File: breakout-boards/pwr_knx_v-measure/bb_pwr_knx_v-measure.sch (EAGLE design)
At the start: 47 parts, among them IC100 BD9G101, T1 BC856, T2 BCP52, T3 BC847

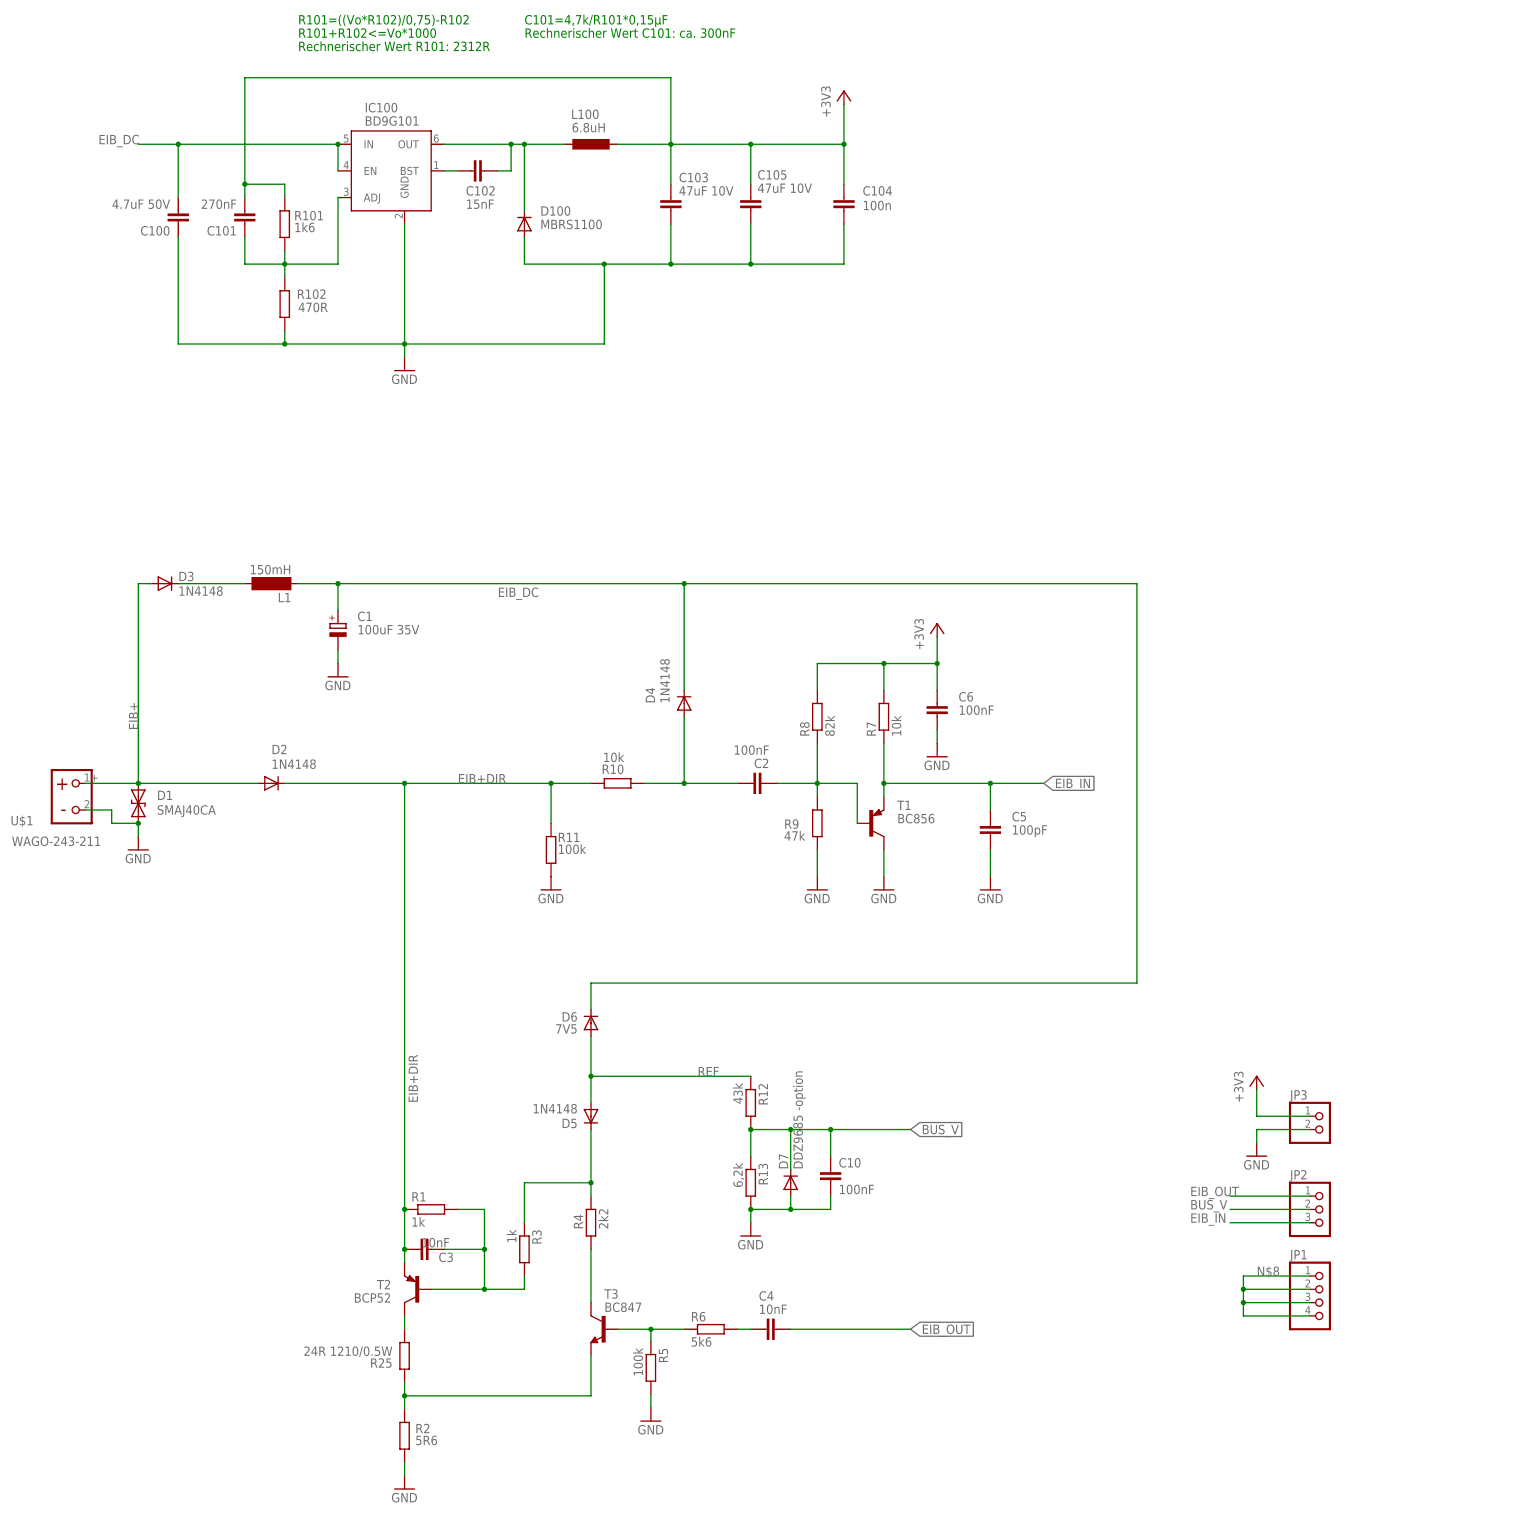
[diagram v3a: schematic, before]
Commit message: [BB_Pwr+KNX] - update pin positions
accidentially committed a version with old pin positions yesterday
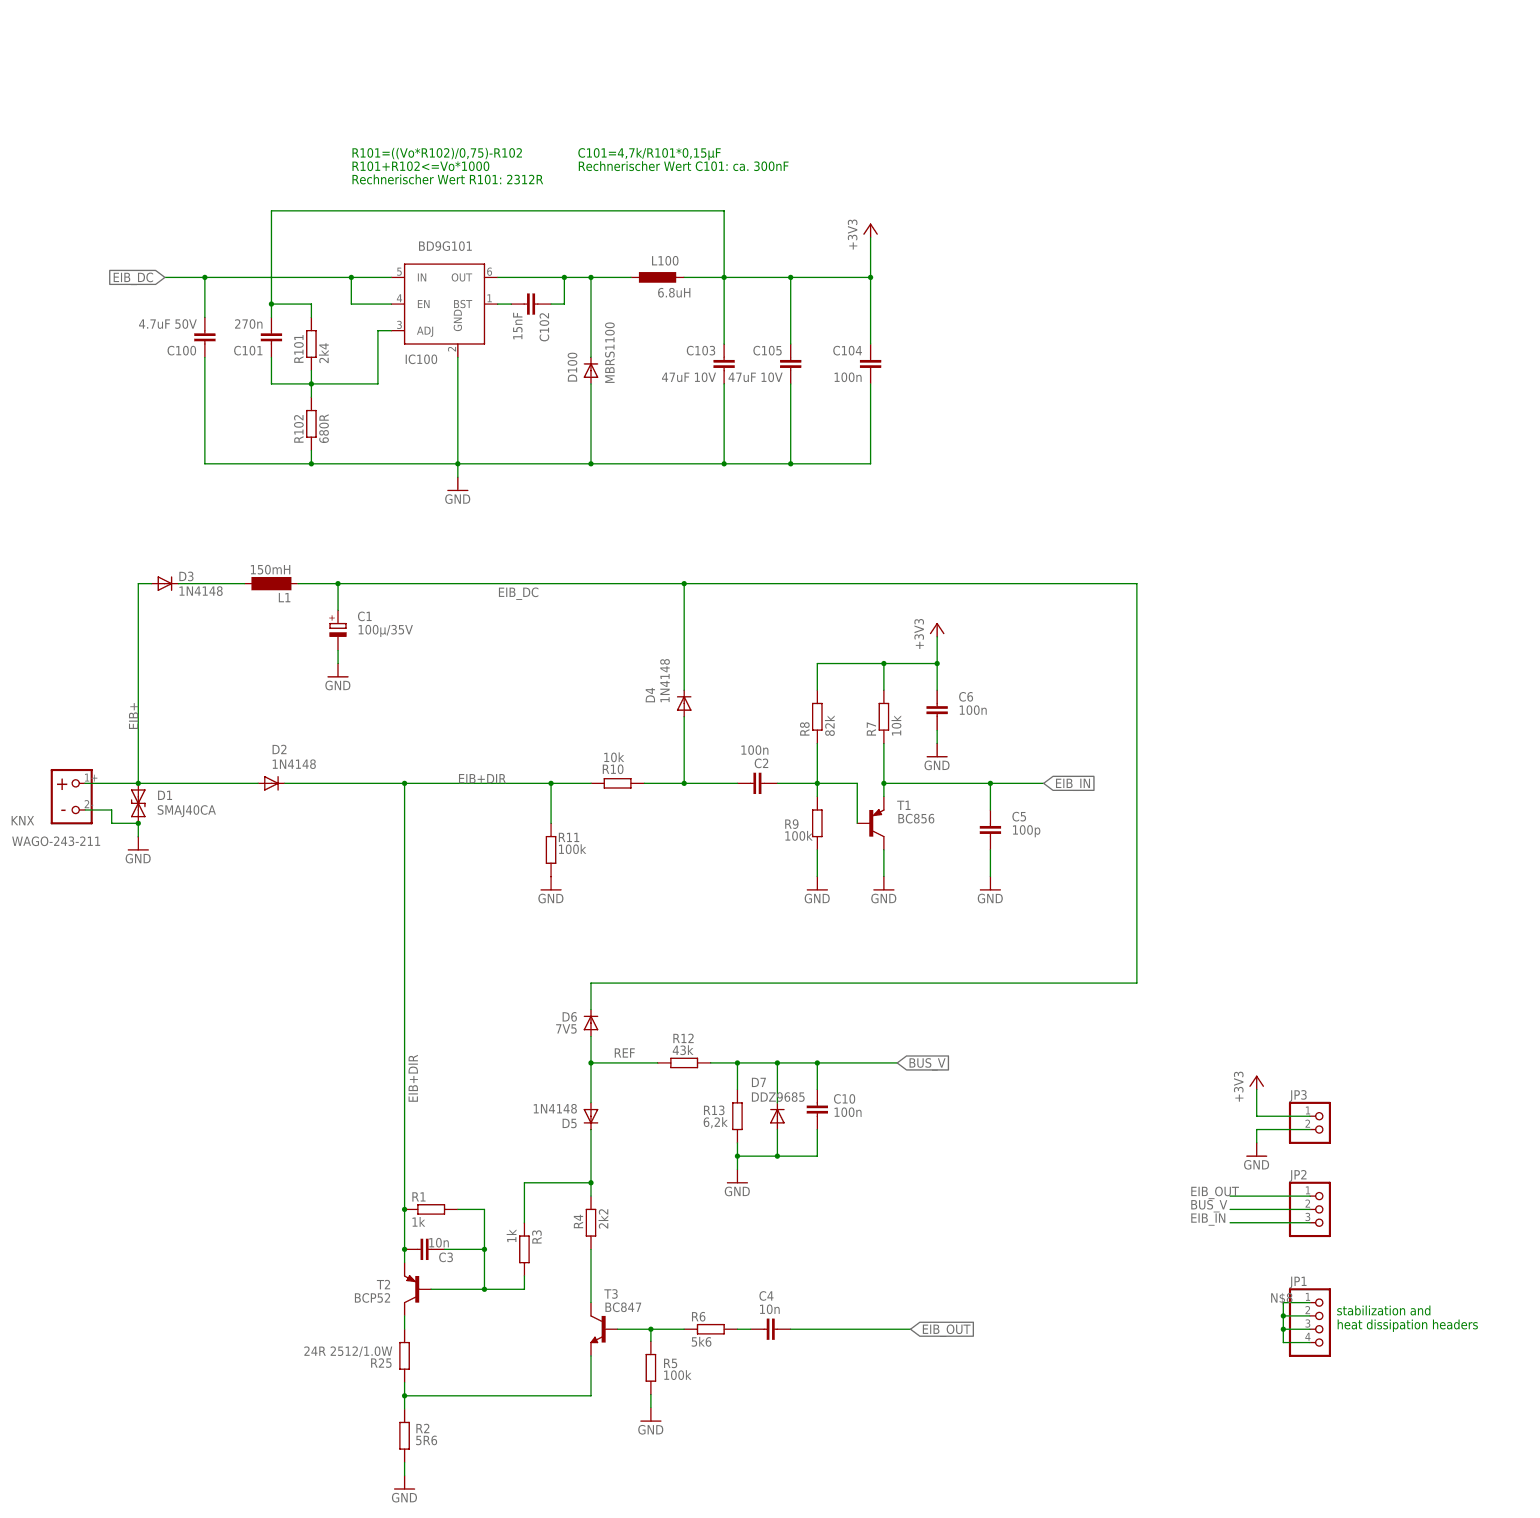
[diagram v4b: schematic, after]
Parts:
- C1: value 100uF 35V -> 100µ/35V
- C10, C2, C6: value 100nF -> 100n
- C100: REICHELT (none) -> X7R-G1206 4,7/50
- C101: value 270nF -> 270n
- C102: REICHELT (none) -> X7R-G0805 15N
- C3, C4: value 10nF -> 10n
- C5: value 100pF -> 100p
- D3: REICHELT (none) -> 1N 4148 SMD
- D7: value DDZ9685 -option -> DDZ9685
- R101: value 1k6 -> 2k4
- R102: value 470R -> 680R
- R25: value 24R 1210/0.5W -> 24R 2512/1.0W
- R6: REICHELT (none) -> SMD-0805 5,60K
- R9: value 47k -> 100k
- T3: REICHELT (none) -> BC 847C SMD
- renumbered U$1 to KNX
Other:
- note added: "stabilization and heat dissipation headers"
- moved on the sheet: C10, C100, C101, C102, C103, C104, C105, D100, D7, IC100, JP1, L100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

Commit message: [BB_Pwr+KNX] - updated docu; updated values of buck components
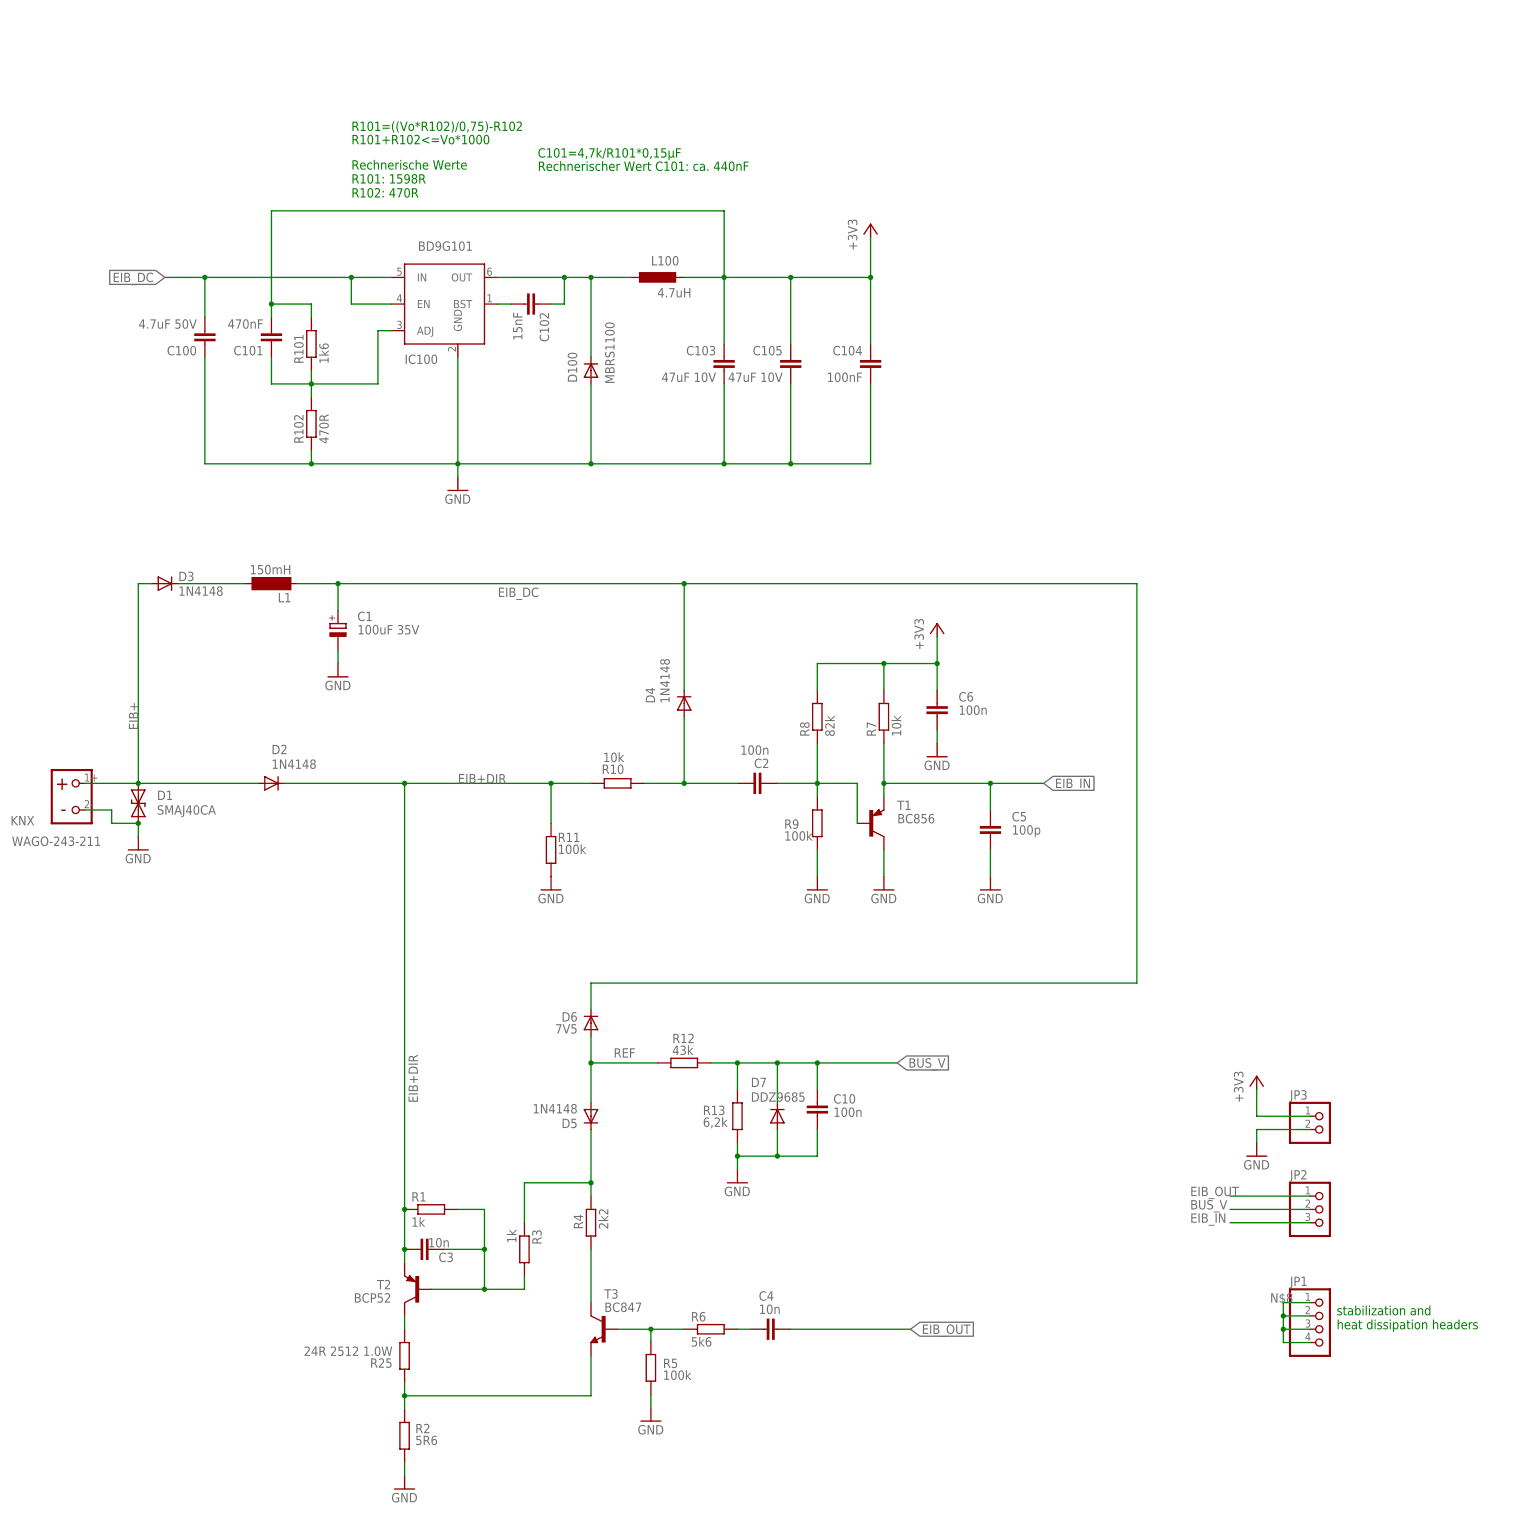
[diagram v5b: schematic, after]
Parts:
- C1: value 100µ/35V -> 100uF 35V
- C101: value 270n -> 470nF
- C104: value 100n -> 100nF
- D3: REICHELT 1N 4148 SMD -> (none)
- L100: value 6.8uH -> 4.7uH
- R101: value 2k4 -> 1k6
- R102: value 680R -> 470R
- R25: value 24R 2512/1.0W -> 24R 2512 1.0W
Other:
- note added: "Rechnerische Werte R101: 1598R R102: 470R"
- note added: "Rechnerischer Wert C101: ca. 440nF"
- note removed: "Rechnerischer Wert C101: ca. 300nF"
- note removed: "Rechnerischer Wert R101: 2312R"
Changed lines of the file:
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@@
 <parts>
 <part name="GND4" library="supply1" deviceset="GND" device=""/>
-<part name="C104" library="rcl" library_urn="urn:adsk.eagle:library:334" deviceset="C-EU" device="C0805" package3d_urn="urn:adsk.eagle:package:23617/2" value="100n">
+<part name="C104" library="rcl" library_urn="urn:adsk.eagle:library:334" deviceset="C-EU" device="C0805" package3d_urn="urn:adsk.eagle:package:23617/2" value="100nF">
 <spice>
 <pinmapping spiceprefix="C">
@@
 <part name="P+3" library="supply1" deviceset="+3V3" device=""/>
 <part name="IC100" library="Stefan_selfbus" deviceset="BD9G101G" device="BD9G101G-SOT23-6" value="BD9G101"/>
-<part name="L100" library="rcl_changed" deviceset="L-EU" device="L4532P" package3d_urn="urn:adsk.eagle:package:23484/1" value="6.8uH">
+<part name="L100" library="rcl_changed" deviceset="L-EU" device="L4532P" package3d_urn="urn:adsk.eagle:package:23484/1" value="4.7uH">
 <spice>
 <pinmapping spiceprefix="L">
@@
 <attribute name="REICHELT" value="X7R-G0805 15N"/>
 </part>
-<part name="R101" library="rcl" library_urn="urn:adsk.eagle:library:334" deviceset="R-EU_" device="R0805" package3d_urn="urn:adsk.eagle:package:23553/2" value="2k4">
-<spice>
-<pinmapping spiceprefix="R">
-<pinmap gate="G$1" pin="1" pinorder="1"/>
-<pinmap gate="G$1" pin="2" pinorder="2"/>
-</pinmapping>
-</spice>
-</part>
-<part name="R102" library="rcl" library_urn="urn:adsk.eagle:library:334" deviceset="R-EU_" device="R0805" package3d_urn="urn:adsk.eagle:package:23553/2" value="680R">
-<spice>
-<pinmapping spiceprefix="R">
-<pinmap gate="G$1" pin="1" pinorder="1"/>
-<pinmap gate="G$1" pin="2" pinorder="2"/>
-</pinmapping>
-</spice>
-</part>
-<part name="C101" library="rcl" library_urn="urn:adsk.eagle:library:334" deviceset="C-EU" device="C0805" package3d_urn="urn:adsk.eagle:package:23617/2" value="270n">
+<part name="R101" library="rcl" library_urn="urn:adsk.eagle:library:334" deviceset="R-EU_" device="R0805" package3d_urn="urn:adsk.eagle:package:23553/2" value="1k6">
+<spice>
+<pinmapping spiceprefix="R">
+<pinmap gate="G$1" pin="1" pinorder="1"/>
+<pinmap gate="G$1" pin="2" pinorder="2"/>
+</pinmapping>
+</spice>
+</part>
+<part name="R102" library="rcl" library_urn="urn:adsk.eagle:library:334" deviceset="R-EU_" device="R0805" package3d_urn="urn:adsk.eagle:package:23553/2" value="470R">
+<spice>
+<pinmapping spiceprefix="R">
+<pinmap gate="G$1" pin="1" pinorder="1"/>
+<pinmap gate="G$1" pin="2" pinorder="2"/>
+</pinmapping>
+</spice>
+</part>
+<part name="C101" library="rcl" library_urn="urn:adsk.eagle:library:334" deviceset="C-EU" device="C0805" package3d_urn="urn:adsk.eagle:package:23617/2" value="470nF">
 <spice>
 <pinmapping spiceprefix="C">
@@
 </spice>
 </part>
-<part name="C1" library="rcl" library_urn="urn:adsk.eagle:library:334" deviceset="CPOL-EU" device="SANYO_SMD_C6" package3d_urn="urn:adsk.eagle:package:23465/1" value="100µ/35V">
+<part name="C1" library="rcl" library_urn="urn:adsk.eagle:library:334" deviceset="CPOL-EU" device="SANYO_SMD_C6" package3d_urn="urn:adsk.eagle:package:23465/1" value="100uF 35V">
 <spice>
 <pinmapping spiceprefix="C">
@@
 <part name="GND1" library="supply1" deviceset="GND" device=""/>
 <part name="D1" library="smaj_10" deviceset="SMAJ*CA" device="" technology="40"/>
-<part name="D3" library="microbuilder" deviceset="DIODE" device="SOD-123" value="1N4148">
-<attribute name="REICHELT" value="1N 4148 SMD"/>
-</part>
+<part name="D3" library="microbuilder" deviceset="DIODE" device="SOD-123" value="1N4148"/>
 <part name="KNX" library="Connector_for_Selfbus-Projects" deviceset="WAGO-243-211" device=""/>
-<part name="R25" library="rcl" library_urn="urn:adsk.eagle:library:334" deviceset="R-EU_" device="R2512" package3d_urn="urn:adsk.eagle:package:23545/2" value="24R  2512/1.0W">
+<part name="R25" library="rcl" library_urn="urn:adsk.eagle:library:334" deviceset="R-EU_" device="R2512" package3d_urn="urn:adsk.eagle:package:23545/2" value="24R  2512 1.0W">
 <spice>
 <pinmapping spiceprefix="R">
@@
 <sheet>
 <plain>
-<text x="73.66" y="259.08" size="1.778" layer="91">R101=((Vo*R102)/0,75)-R102</text>
-<text x="73.66" y="256.54" size="1.778" layer="91">R101+R102&lt;=Vo*1000</text>
-<text x="73.66" y="254" size="1.778" layer="91">Rechnerischer Wert R101: 2312R</text>
-<text x="116.84" y="259.08" size="1.778" layer="91">C101=4,7k/R101*0,15µF</text>
-<text x="116.84" y="256.54" size="1.778" layer="91">Rechnerischer Wert C101: ca. 300nF</text>
+<text x="73.66" y="264.16" size="1.778" layer="91">R101=((Vo*R102)/0,75)-R102</text>
+<text x="73.66" y="261.62" size="1.778" layer="91">R101+R102&lt;=Vo*1000</text>
+<text x="73.66" y="251.46" size="1.778" layer="91">Rechnerische Werte
+R101: 1598R
+R102: 470R</text>
+<text x="109.22" y="259.08" size="1.778" layer="91">C101=4,7k/R101*0,15µF</text>
+<text x="109.22" y="256.54" size="1.778" layer="91">Rechnerischer Wert C101: ca. 440nF</text>
 <text x="261.62" y="35.56" size="1.778" layer="91">stabilization and
 heat dissipation headers</text>
@@
 </instance>
 <instance part="D3" gate="G$1" x="38.1" y="177.8" smashed="yes">
-<attribute name="REICHELT" x="38.1" y="177.8" size="1.778" layer="96" display="off"/>
 <attribute name="NAME" x="40.64" y="178.2826" size="1.778" layer="95"/>
 <attribute name="VALUE" x="40.64" y="175.4886" size="1.778" layer="96"/>
